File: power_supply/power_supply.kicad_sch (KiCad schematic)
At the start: 17 parts, among them Q1 TIP122, T1 35VAC - 3A, U1 CA3140

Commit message: Considerações Finais - Circuito da fonte + Amplificador
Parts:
- added J1: Alimentação, symbol Connector_Generic:Conn_01x02
- R2: value 1K0 -> 750R
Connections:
- net at D6.1 (K), R2.2, RV1.1: no longer U1.3 (+)
- net at RV1.2: now also U1.3 (+)
- net at T1.1 (AA): now also J1.2 (Pin_2)
- net at T1.2 (AB): now also J1.1 (Pin_1)
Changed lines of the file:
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@@
   (junction (at 86.868 27.686) (diameter 0) (color 0 0 0 0)
-  )
-  (junction (at 195.58 42.926) (diameter 0) (color 0 0 0 0)
   )
   (junction (at 172.974 32.766) (diameter 0) (color 0 0 0 0)
@@
   (no_connect (at 221.234 37.846))
   (no_connect (at 218.694 53.086))
-  (wire (pts (xy 195.834 63.246) (xy 195.834 63.754))
-    (stroke (width 0) (type default))
-  )
   (wire (pts (xy 172.974 32.766) (xy 172.974 34.29))
     (stroke (width 0) (type default))
@@
     (stroke (width 0) (type default))
   )
-  (wire (pts (xy 195.58 63.246) (xy 195.58 52.324))
+  (wire (pts (xy 195.58 52.324) (xy 195.58 63.754))
     (stroke (width 0) (type default))
   )
@@
     (stroke (width 0) (type default))
   )
+  (wire (pts (xy 33.274 31.242) (xy 36.322 31.242))
+    (stroke (width 0) (type default))
+  )
   (wire (pts (xy 141.478 32.766) (xy 141.478 39.878))
     (stroke (width 0) (type default))
   )
-  (wire (pts (xy 42.164 27.178) (xy 47.752 27.178))
-    (stroke (width 0) (type default))
-  )
-  (wire (pts (xy 195.834 63.246) (xy 195.58 63.246))
+  (wire (pts (xy 36.322 27.178) (xy 47.752 27.178))
     (stroke (width 0) (type default))
   )
@@
     (stroke (width 0) (type default))
   )
-  (wire (pts (xy 195.58 42.926) (xy 211.074 42.926))
-    (stroke (width 0) (type default))
-  )
   (wire (pts (xy 123.19 32.766) (xy 132.334 32.766))
     (stroke (width 0) (type default))
@@
     (stroke (width 0) (type default))
   )
-  (wire (pts (xy 42.164 37.338) (xy 47.752 37.338))
+  (wire (pts (xy 36.322 37.338) (xy 47.752 37.338))
     (stroke (width 0) (type default))
   )
@@
     (stroke (width 0) (type default))
   )
+  (wire (pts (xy 36.322 31.242) (xy 36.322 27.178))
+    (stroke (width 0) (type default))
+  )
   (wire (pts (xy 99.314 32.766) (xy 99.314 37.338))
     (stroke (width 0) (type default))
@@
     (stroke (width 0) (type default))
   )
+  (wire (pts (xy 36.322 33.782) (xy 36.322 37.338))
+    (stroke (width 0) (type default))
+  )
+  (wire (pts (xy 199.39 48.514) (xy 204.724 48.514))
+    (stroke (width 0) (type default))
+  )
+  (wire (pts (xy 204.724 42.926) (xy 211.074 42.926))
+    (stroke (width 0) (type default))
+  )
   (wire (pts (xy 107.95 52.832) (xy 107.95 63.246))
     (stroke (width 0) (type default))
@@
     (stroke (width 0) (type default))
   )
+  (wire (pts (xy 33.274 33.782) (xy 36.322 33.782))
+    (stroke (width 0) (type default))
+  )
   (wire (pts (xy 216.154 37.846) (xy 216.154 32.766))
     (stroke (width 0) (type default))
@@
   )
   (wire (pts (xy 234.188 51.054) (xy 241.808 51.054))
+    (stroke (width 0) (type default))
+  )
+  (wire (pts (xy 204.724 48.514) (xy 204.724 42.926))
     (stroke (width 0) (type default))
   )
@@
       (effects (font (size 1.27 1.27)) (justify left))
     )
-    (property "Value" "1K0" (at 174.244 38.862 0)
+    (property "Value" "750R" (at 174.244 38.862 0)
       (effects (font (size 1.27 1.27)) (justify left))
     )
@@
     )
   )
-  (symbol (lib_id "power:GNDREF") (at 195.834 63.754 0) (unit 1)
-    (in_bom yes) (on_board yes) (dnp no)
-    (property "Reference" "#PWR08" (at 195.834 70.104 0)
-      (effects (font (size 1.27 1.27)) hide)
-    )
-    (property "Value" "GNDREF" (at 195.834 67.818 0)
-      (effects (font (size 1.27 1.27)))
-    )
-    (property "Footprint" "" (at 195.834 63.754 0)
-      (effects (font (size 1.27 1.27)) hide)
-    )
-    (property "Datasheet" "" (at 195.834 63.754 0)
+  (symbol (lib_id "power:GNDREF") (at 195.58 63.754 0) (unit 1)
+    (in_bom yes) (on_board yes) (dnp no)
+    (property "Reference" "#PWR08" (at 195.58 70.104 0)
+      (effects (font (size 1.27 1.27)) hide)
+    )
+    (property "Value" "GNDREF" (at 195.58 67.818 0)
+      (effects (font (size 1.27 1.27)))
+    )
+    (property "Footprint" "" (at 195.58 63.754 0)
+      (effects (font (size 1.27 1.27)) hide)
+    )
+    (property "Datasheet" "" (at 195.58 63.754 0)
       (effects (font (size 1.27 1.27)) hide)
     )
@@
         )
       )
+    )
+  )
+  (symbol (lib_id "Connector_Generic:Conn_01x02") (at 28.194 33.782 180) (unit 1)
+    (in_bom yes) (on_board yes) (dnp no)
+    (property "Reference" "J1" (at 28.194 28.448 0)
+      (effects (font (size 1.27 1.27)))
+    )
+    (property "Value" "Alimentação" (at 28.194 36.322 0)
+      (effects (font (size 1.27 1.27)))
+    )
+    (property "Footprint" "" (at 28.194 33.782 0)
+      (effects (font (size 1.27 1.27)) hide)
+    )
+    (property "Datasheet" "~" (at 28.194 33.782 0)
+      (effects (font (size 1.27 1.27)) hide)
+    )
+    (pin "1")
+    (pin "2")
+    (instances
+      (project "power_supply"
+        (path "/22e05a20-d029-41db-9dfe-dd14f5d3b1be"
+          (reference "J1") (unit 1)
+        )
+      )

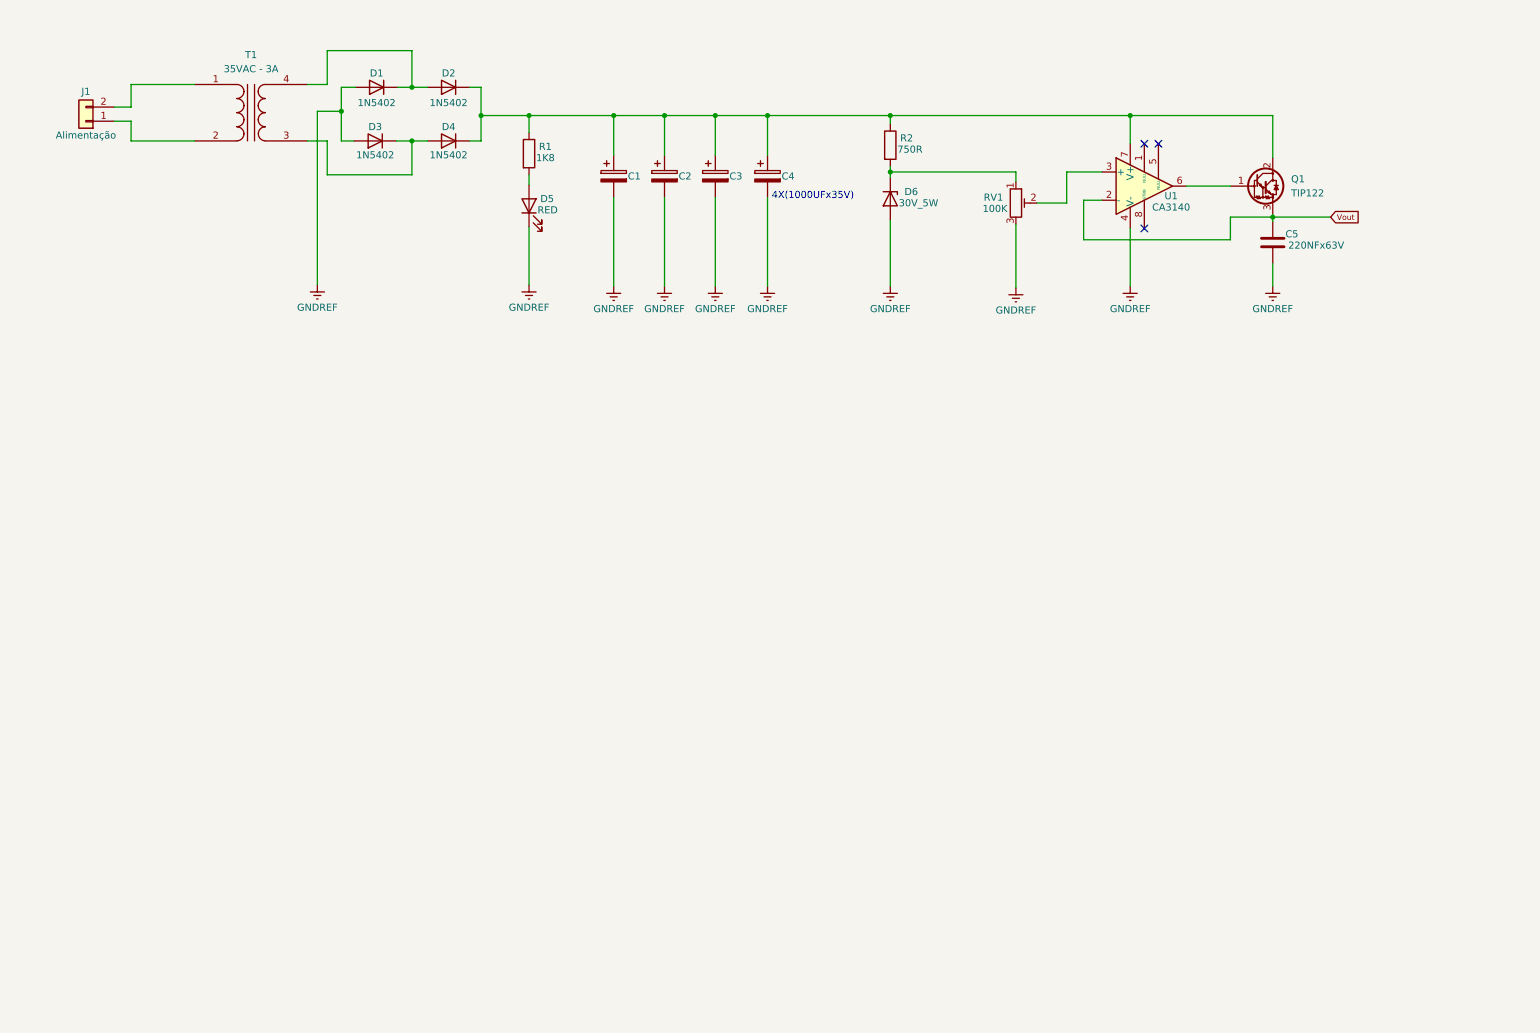
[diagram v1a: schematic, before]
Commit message: Adicionado o circuito dos reguladores de tensão, bem como o circuito do ICL para controle do voltímetro via display de 7 segmentos.
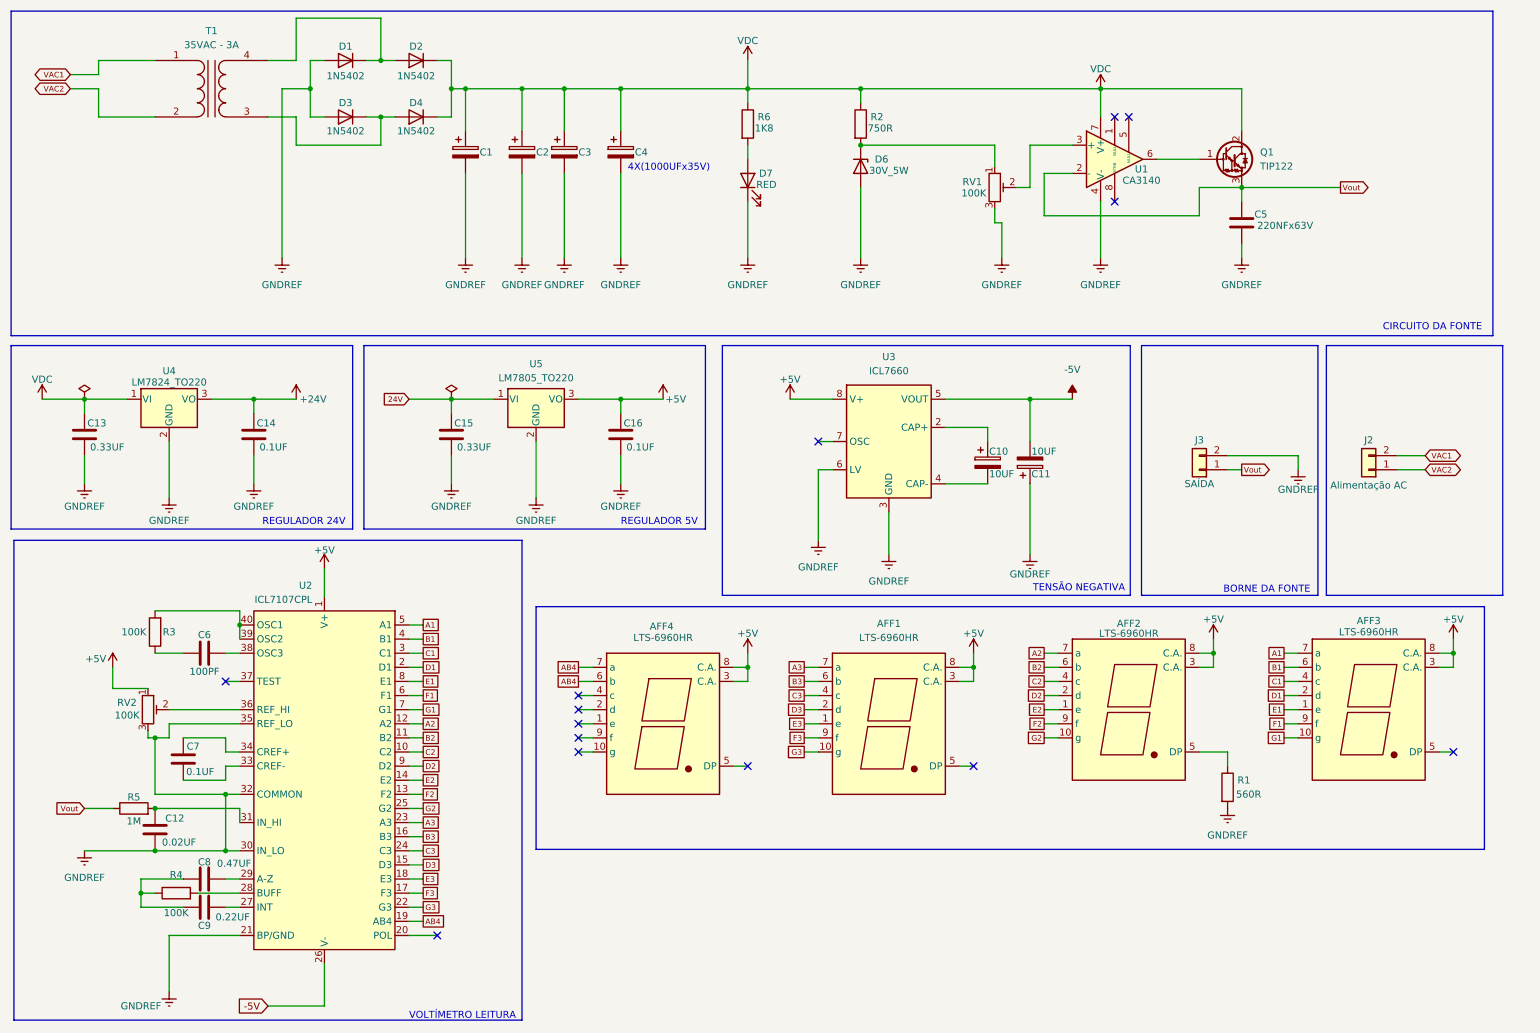
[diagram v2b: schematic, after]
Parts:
- removed D5: RED, symbol Device:LED
- removed J1: Alimentação, symbol Connector_Generic:Conn_01x02
- added AFF1, AFF2, AFF3, AFF4: LTS-6960HR, Display_7Segment:7SegmentLED_LTS6760_LTS6780, symbol Display_Character:LTS-6960HR
- added C10, C11: 10UF, symbol Device:C_Polarized
- added C12: 0.02UF, symbol Device:C
- added C13, C15: 0.33UF, symbol Device:C
- added C14, C16, C7: 0.1UF, symbol Device:C
- added C6: 100PF, symbol Device:C
- added C8: 0.47UF, symbol Device:C
- added C9: 0.22UF, symbol Device:C
- added D7: RED, symbol Device:LED
- added J2: Alimentação AC, symbol Connector_Generic:Conn_01x02
- added J3: SAÍDA, symbol Connector_Generic:Conn_01x02
- added R3, R4: 100K, symbol Device:R
- added R5: 1M, symbol Device:R
- added R6: 1K8, symbol Device:R
- added RV2: 100K, symbol Device:R_Potentiometer_Trim
- added U2: ICL7107CPL, Package_DIP:DIP-40_W15.24mm_Socket_LongPads, symbol Analog_ADC:ICL7107CPL
- added U3: ICL7660, Package_SO:SOIC-8_3.9x4.9mm_P1.27mm, symbol Regulator_SwitchedCapacitor:ICL7660
- added U4: LM7824_TO220, Package_TO_SOT_THT:TO-220-3_Vertical, symbol Regulator_Linear:LM7824_TO220
- added U5: LM7805_TO220, Package_TO_SOT_THT:TO-220-3_Vertical, symbol Regulator_Linear:LM7805_TO220
- R1: value 1K8 -> 560R
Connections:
- net GNDREF: now also R1.2, C11.1, C12.2, C13.2, C14.2, C15.2, C16.2, D7.1 (K), J3.2 (Pin_2), RV2.3, U2.21 (BP/GND), U2.30 (IN_LO), U2.32 (COMMON), U2.35 (REF_LO), U3.3 (GND), U3.6 (LV), U4.2 (GND), U5.2 (GND)
- net Vout: now also J3.1 (Pin_1), R5.1
- net VDC: now reaches C1.1, C2.1, C3.1, C4.1, D2.1 (K), D4.1 (K), Q1.2 (C), R2.1, U1.7 (V+)
- net VDC: now also C13.1, R6.1, U4.1 (VI); no longer R1.1
- net VAC1: now reaches T1.1 (AA)
- net VAC1: now also J2.2 (Pin_2)
- net VAC2: now reaches T1.2 (AB)
- net VAC2: now also J2.1 (Pin_1)
- new net: C6.2, R3.1
- new net: R3.2, U2.39 (OSC2), U2.40 (OSC1)
- new net: D7.2 (A), R6.2
- new net: C10.1, U3.2 (CAP+)
- new net: C10.2, U3.4 (CAP-)
- new net: C12.1, R5.2, U2.31 (IN_HI)
- new net: AFF2.5 (DP), R1.1
- new net: RV2.2, U2.36 (REF_HI)
- new net: C6.1, U2.38 (OSC3)
- new net: C8.1, C9.1, R4.1
- new net: R4.2, U2.28 (BUFF)
- new net: C9.2, U2.27 (INT)
- new net: C7.1, U2.34 (CREF+)
- new net: C7.2, U2.33 (CREF-)
- new net: C8.2, U2.29 (A-Z)
- new net +24V: C14.1, U4.3 (VO)
- new net +5V: AFF1.3 (C.A.), AFF1.8 (C.A.), AFF2.3 (C.A.), AFF2.8 (C.A.), AFF3.3 (C.A.), AFF3.8 (C.A.), AFF4.3 (C.A.), AFF4.8 (C.A.), C16.1, RV2.1, U2.1 (V+), U3.8 (V+), U5.3 (VO)
- new net -5V: C11.2, U2.26 (V-), U3.5 (VOUT)
- new net 24V: C15.1, U5.1 (VI)
- new net A1: AFF3.7 (a), U2.5 (A1)
- new net A2: AFF2.7 (a), U2.12 (A2)
- new net A3: AFF1.7 (a), U2.23 (A3)
- new net AB4: AFF4.6 (b), AFF4.7 (a), U2.19 (AB4)
- new net B1: AFF3.6 (b), U2.4 (B1)
- new net B2: AFF2.6 (b), U2.11 (B2)
- new net B3: AFF1.6 (b), U2.16 (B3)
- new net C1: AFF3.4 (c), U2.3 (C1)
- new net C2: AFF2.4 (c), U2.10 (C2)
- new net C3: AFF1.4 (c), U2.24 (C3)
- new net D1: AFF3.2 (d), U2.2 (D1)
- new net D2: AFF2.2 (d), U2.9 (D2)
- new net D3: AFF1.2 (d), U2.15 (D3)
- new net E1: AFF3.1 (e), U2.8 (E1)
- new net E2: AFF2.1 (e), U2.14 (E2)
- new net E3: AFF1.1 (e), U2.18 (E3)
- new net F1: AFF3.9 (f), U2.6 (F1)
- new net F2: AFF2.9 (f), U2.13 (F2)
- new net F3: AFF1.9 (f), U2.17 (F3)
- new net G1: AFF3.10 (g), U2.7 (G1)
- new net G2: AFF2.10 (g), U2.25 (G2)
- new net G3: AFF1.10 (g), U2.22 (G3)
- no-connect marks 3 -> 14
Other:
- note added: "BORNE DA FONTE"
- note added: "CIRCUITO DA FONTE"
- note added: "REGULADOR 24V"
- note added: "REGULADOR 5V"
- note added: "TENSÃO NEGATIVA"
- note added: "VOLTÍMETRO LEITURA"
- moved on the sheet: C1, C2, C3, C4, C5, D1, D2, D3, D4, D6, Q1, R2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

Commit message: Finalização do esquemático, seleção de footprints e organização dos componentes no layout
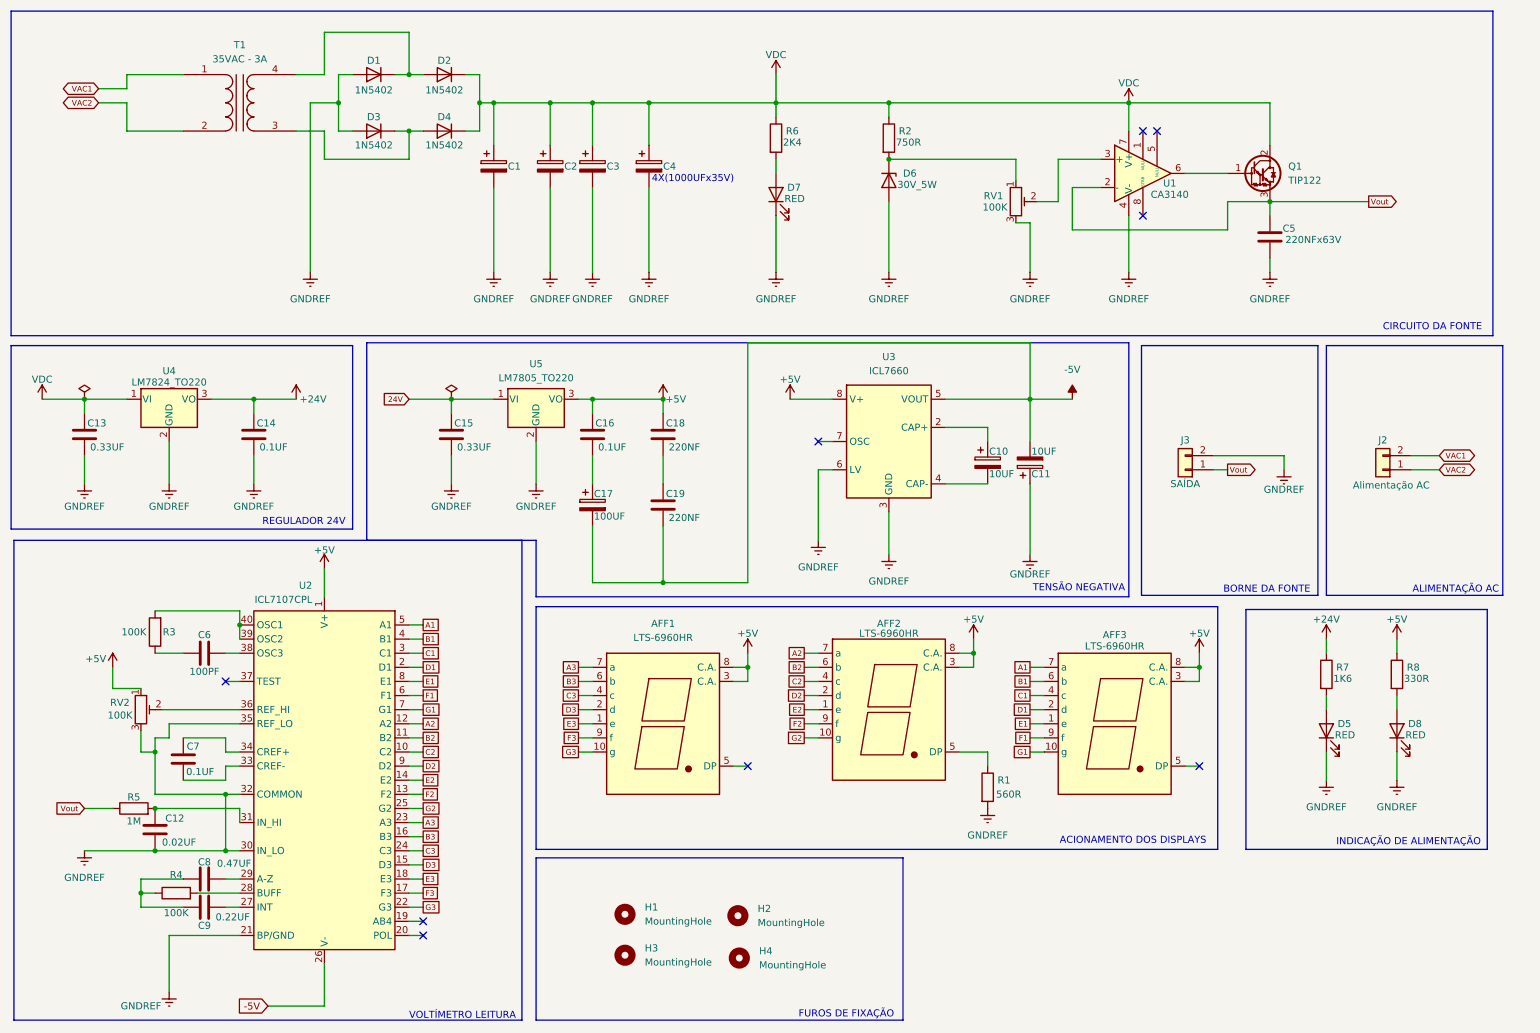
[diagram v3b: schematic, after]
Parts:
- removed AFF4: LTS-6960HR, Display_7Segment:7SegmentLED_LTS6760_LTS6780, symbol Display_Character:LTS-6960HR
- added C17: 100UF, Capacitor_SMD:CP_Elec_6.3x7.7, symbol Device:C_Polarized
- added C18, C19: 220NF, Capacitor_SMD:C_1206_3216Metric, symbol Device:C
- added D5, D8: RED, LED_SMD:LED_1206_3216Metric, symbol Device:LED
- added H1, H2, H3, H4: MountingHole, MountingHole:MountingHole_3.2mm_M3, symbol Mechanical:MountingHole
- added R7: 1K6, Resistor_SMD:R_1206_3216Metric, symbol Device:R
- added R8: 330R, Resistor_SMD:R_1206_3216Metric, symbol Device:R
- C1, C2, C3, C4: footprint (none) -> Capacitor_SMD:CP_Elec_16x17.5
- C10, C11: footprint (none) -> Capacitor_SMD:CP_Elec_5x5.4
- C12, C13, C14, C15, C16, C5, C6, C7, C8, C9: footprint (none) -> Capacitor_SMD:C_1206_3216Metric
- D6: footprint (none) -> Diode_SMD:D_SMA
- D7: footprint (none) -> LED_SMD:LED_1206_3216Metric
- J2: footprint (none) -> Connector_Molex:Molex_KK-396_5273-02A_1x02_P3.96mm_Vertical
- J3: footprint (none) -> Connector:Banana_Jack_2Pin
- R1, R2, R3, R4, R5: footprint (none) -> Resistor_SMD:R_1206_3216Metric
- R6: value 1K8 -> 2K4; footprint (none) -> Resistor_SMD:R_1206_3216Metric
- RV1: footprint (none) -> Potentiometer_THT:Potentiometer_Vishay_248GJ-249GJ_Single_Horizontal
- RV2: footprint (none) -> Potentiometer_THT:Potentiometer_Vishay_T73YP_Vertical
- T1: footprint (none) -> Transformer_THT:Transformer_37x44
- U1: footprint (none) -> Package_SO:SOIC-8_3.9x4.9mm_P1.27mm
- U2: footprint Package_DIP:DIP-40_W15.24mm_Socket_LongPads -> Package_QFP:MQFP-44_10x10mm_P0.8mm
- U4, U5: footprint Package_TO_SOT_THT:TO-220-3_Vertical -> Package_TO_SOT_THT:TO-220-3_Horizontal_TabDown
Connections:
- net +24V: now also R7.1
- net +5V: now also C18.1, R8.1
- net -5V: now also C17.2, C19.2
- net GNDREF: now also D5.1 (K), D8.1 (K); no longer C16.2
- net AB4: no longer names the net of U2.19 (AB4)
- new net: D8.2 (A), R8.2
- new net: C16.2, C17.1
- new net: C18.2, C19.1
- new net: D5.2 (A), R7.2
- no-connect marks 14 -> 9
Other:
- note added: "ACIONAMENTO DOS DISPLAYS"
- note added: "ALIMENTAÇÃO AC"
- note added: "FUROS DE FIXAÇÃO"
- note added: "INDICAÇÃO DE ALIMENTAÇÃO"
- note removed: "REGULADOR 5V"
- moved on the sheet: AFF1, AFF2, AFF3, C1, C16, C2, C3, C4, C5, D1, D2, D3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

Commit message: Retira do Transformador On-Board para externo, troca de footprint para um conector Molex de 4 vias (3.96mm); Início do roteamento das trilhas e isolação dos planos GND.
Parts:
- T1: footprint Transformer_THT:Transformer_37x44 -> Connector_Molex:Molex_KK-396_5273-04A_1x04_P3.96mm_Vertical
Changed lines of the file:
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@@
       (effects (font (size 1.27 1.27)))
     )
-    (property "Footprint" "Transformer_THT:Transformer_37x44" (at 55.88 30.48 0)
+    (property "Footprint" "Connector_Molex:Molex_KK-396_5273-04A_1x04_P3.96mm_Vertical" (at 55.88 30.48 0)
       (effects (font (size 1.27 1.27)) hide)
     )
